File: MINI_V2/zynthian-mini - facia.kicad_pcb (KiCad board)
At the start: 2 copper layers, 163 x 120 mm, 2 parts

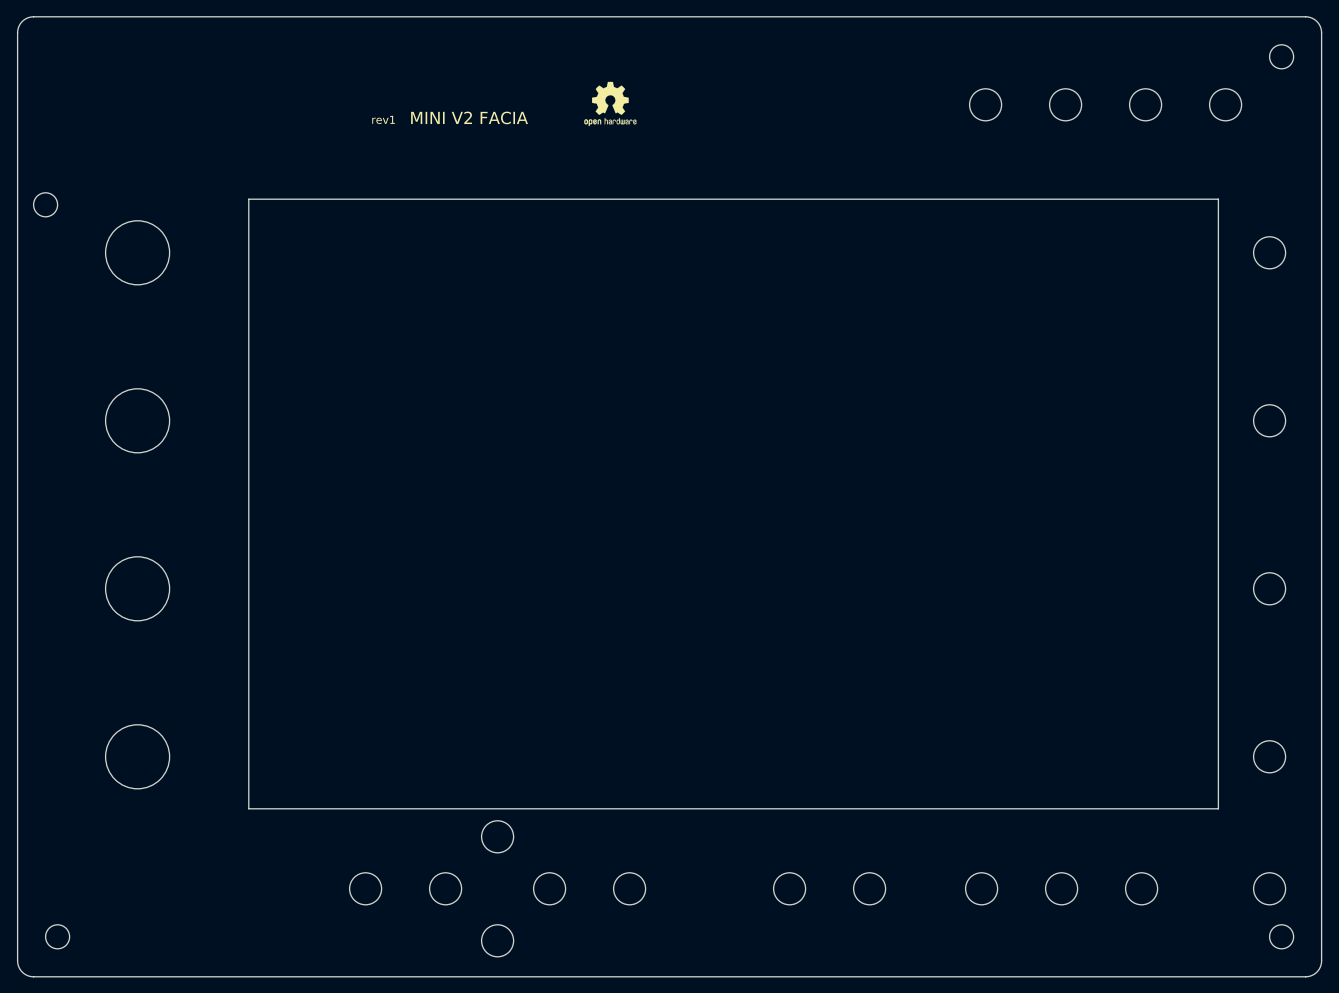
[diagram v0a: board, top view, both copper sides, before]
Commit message: updated facia PCB so that it include copper layer reqruied to pass production requirements
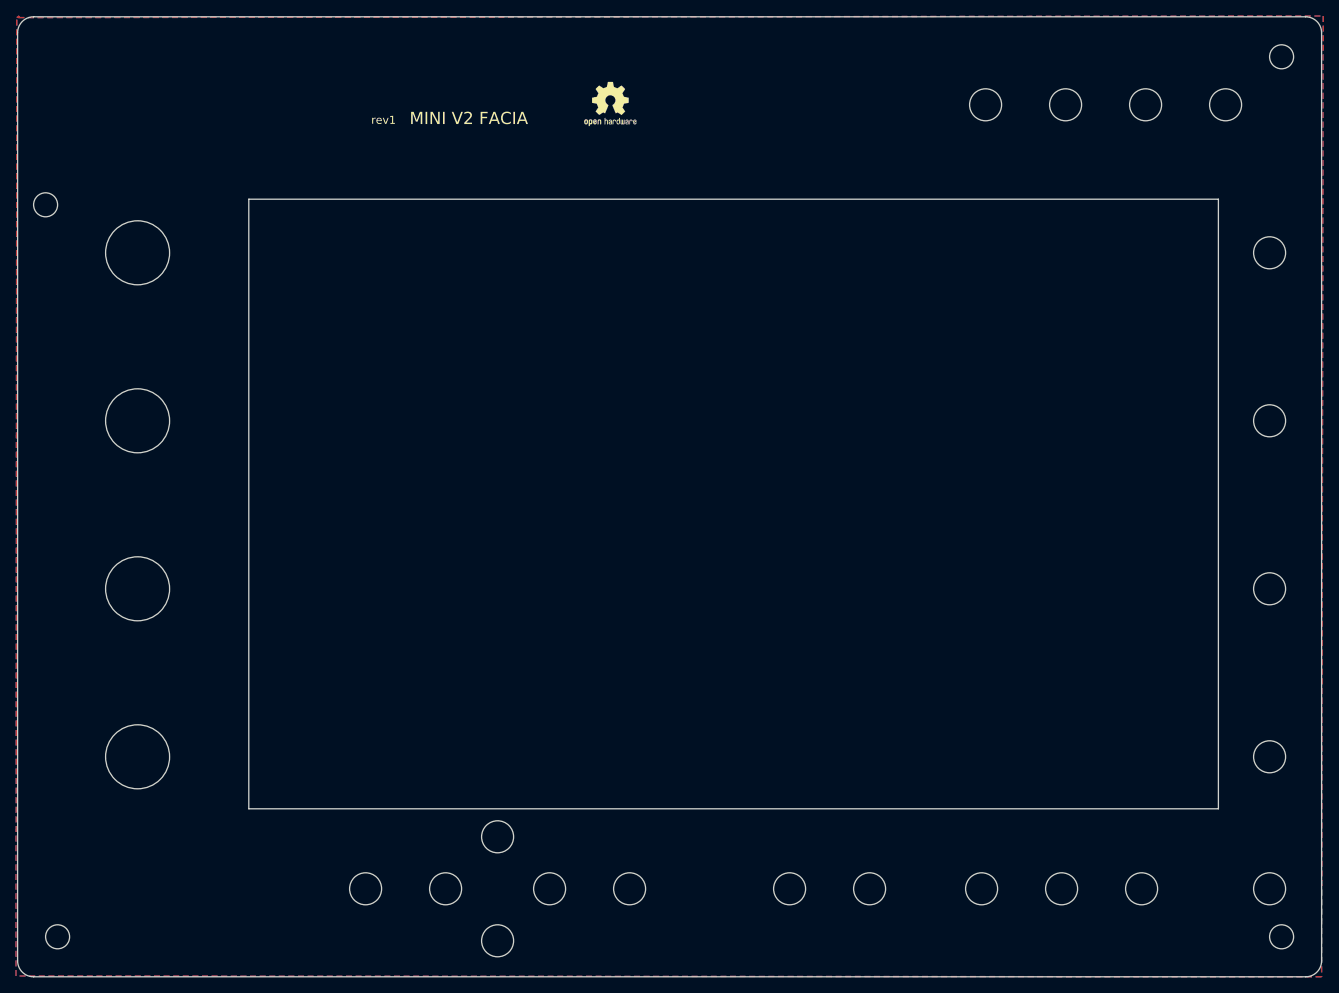
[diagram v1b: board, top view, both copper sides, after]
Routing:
- added copper zone on B.Cu, net (none)
- added copper zone on F.Cu, net (none)
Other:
- board text removed: "AUDIO OUT"
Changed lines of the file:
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@@
 			(drillshape 0)
 			(scaleselection 1)
-			(outputdirectory "gerber-v2/")
+			(outputdirectory "production/facia")
 		)
 	)
@@
 		(layer "Edge.Cuts")
 	)
-	(gr_text "AUDIO OUT"
-		(at 194.8193 106.0736 270)
-		(layer "B.SilkS")
-		(effects
-			(font
-				(size 1 1)
-				(thickness 0.25)
-			)
-			(justify mirror)
-		)
-	)
 	(gr_text "rev1"
 		(at 77.6193 48.8736 0)
@@
 			(extension_offset 0.5) keep_text_aligned)
 	)
+	(zone
+		(net 0)
+		(net_name "")
+		(layers "F&B.Cu")
+		(hatch edge 0.5)
+		(connect_pads
+			(clearance 0.5)
+		)
+		(min_thickness 0.25)
+		(filled_areas_thickness no)
+		(fill yes
+			(thermal_gap 0.5)
+			(thermal_bridge_width 0.5)
+			(island_removal_mode 1)
+			(island_area_min 10)
+		)
+		(polygon
+			(pts
+				(xy 33.5193 35.4736) (xy 196.6193 35.2736) (xy 196.4193 155.3736) (xy 33.2193 155.2736) (xy 33.3193 35.4736)
+				(xy 33.6193 35.2736)
+			)
+		)
+	)
 	(group ""
